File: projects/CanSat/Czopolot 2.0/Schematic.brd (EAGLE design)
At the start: 50.5 x 30.5 mm, 98 parts

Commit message: Microcontroller and sensors done...
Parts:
- removed C40, C41: 100n, Unified:C0603
- removed C43, C44: 10u, Unified:C0603
- removed MOTL, MOTR: MOTOR, Unified:2X_JST
- removed R1, R13: 4.7k, Unified:R0603
- removed R12, R14, R3: 100k, Unified:R0603
- removed R40, R41, R7, R70, R71, R72, R8, R9: 10k, Unified:R0603
- removed R5: 560R, Unified:R0603
- removed RN1: 560R, SobieskiSat2:0603-ARC
- added BTN_USR1: PUSH-SWITCH, SobieskiSat2:SWITCH_SMD
- added U$12: TC78H653FTG, SobieskiSat2:QFN50P300X300X90-17T170N
- added U$13: MOTORJST_SMD, Unified:2X_JSTSMD_F
- added U$16, U$26: RESISTORARRAY, SobieskiSat2:0603-ARC
- added U$17, U$18: CONNECTOR_F_X2_JST_SMD, Unified:2X_JSTSMD_F
- added U$19, U$20, U$24, U$25: CONNECTOR_F_X3_JST_SMD, Unified:3X_JSTSMD_F
- added X1: FH12-24S-0.5SH, con-hirose:FH12-24S-0.5SH
- BAT_PACK: device SobieskiSat2:BAT_THT -> SobieskiSat2:2X_JSTSMD_F
- BTN_DFU: value PUSH-SWITCHDIP -> SLIDE-SWITCH; device SobieskiSat2:2X_JST -> SobieskiSat2:SLIDE-SWITCH
- U$14: value DRV8838 -> MOTORJST_SMD; device SobieskiSat2:SON50P200X200X80-9T90X160N -> Unified:2X_JSTSMD_F
- U$15: value DRV8838 -> RESISTORARRAY; device SobieskiSat2:SON50P200X200X80-9T90X160N -> SobieskiSat2:0603-ARC
- U$4: value SLIDE-SWITCH -> RESISTORARRAY; device SobieskiSat2:SLIDE-SWITCH -> SobieskiSat2:0603-ARC
- U$7: value USB-C -> USB2.0; device SobieskiSat2:USB-C -> SobieskiSat2:USB-C(2)
- moved U$23 35.9 mm to (67.8, 25.8)
- moved LM3940IMP 35.6 mm to (46.0, 18.8), flipped to the bottom, turned to 90 degrees
- moved U$14 34.6 mm to (35.8, 3.50), flipped to the bottom, turned to 180 degrees
- moved BAT_PACK 34.3 mm to (58.5, 3.75)
- moved U$22 33.9 mm to (67.8, 21.4)
- moved LEDA 33.6 mm to (4.75, 28.8), turned to 0 degrees
- moved C31 33.4 mm to (43.5, 13.2)
- moved C30 32.2 mm to (51.2, 17.2), turned to 90 degrees
- moved LEDB 31.9 mm to (6.75, 28.8), turned to 0 degrees
- moved C2 31.6 mm to (49.0, 13.2), flipped to the bottom, turned to 0 degrees
- moved C10 30.8 mm to (50.0, 14.5), turned to 0 degrees
- moved CBK 30.6 mm to (2.00, 25.5), flipped to the top, turned to 90 degrees
- moved LEDC 30.3 mm to (8.75, 28.8), turned to 0 degrees
- moved C23 30.2 mm to (46.0, 10.5)
- moved C21 29.6 mm to (54.8, 20.0)
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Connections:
- removed net EN_L: U$1.15, U$14.5
- removed net EN_R: U$1.17, U$15.5
- removed net GPIO_S1: U$1.26, U$11.6
- removed net GPIO_S2: U$1.27, U$11.10
- removed net N$23: C70.2, U$9.10
- removed net N$31: R40.1, U$14.7
- removed net N$34: MOTR.P$2, U$15.2
- removed net N$36: MOTR.P$1, U$15.3
- removed net N$40: R41.1, U$15.7
- removed net PH_L: U$1.14, U$14.6
- removed net PH_R: U$1.16, U$15.6
- new net EN_1: U$1.33
- new net EN_2: U$1.34
- new net EN_3: U$1.35
- new net EN_4: U$1.36
- new net MPU_REG: C70.2, U$9.10, U$9.14
- new net N$25: R0.1
- new net N$7: BTN_USR.P$1, BTN_USR.P$4, U$16.4
- new net PWM_1: U$1.27
- new net PWM_2: U$1.26
- new net PWM_3: U$1.37
- new net PWM_4: U$1.38
- net 43_D0: now also U$1.24; no longer U$1.25
- net 43_D1: now also U$1.25; no longer U$1.24
- net 43_MOSI: now also U$26.8; no longer R3.2
- net 43_NSS: now also U$1.2; no longer U$1.61
- net 43_RST: now also U$1.50; no longer R2.2, U$1.28
- net BAT: now also BAT_PACK.+; no longer BAT_PACK.P$2, C40.2, C43.2, U$14.1, U$15.1
- net BMP_SDI: now also U$26.7; no longer R9.1
- net BMP_SDO: now also U$26.6; no longer R8.2
- net DFU: now also U$16.7; no longer BTN_DFU.P$2, R12.1
- net GND: now also BAT_PACK.-, U$7.A1, U$7.A12, U$7.B1, U$7.B12, U$7.MID@1, U$7.MID@2, U$9.5; no longer BAT_PACK.P$1, BTN_USR.P$1, BTN_USR.P$4, C40.1, C41.1, C43.1, C44.1, R0.1, R12.2, R8.1, U$14.4, U$14.9, U$15.4, U$15.9, U$7.A$1, U$7.A$12, U$7.B$1, U$7.B$12, U$7.N$1, U$7.N$2, U$7.N$3, U$7.N$4, U$7.N$5, U$7.N$6
- net GPIO_RX: no longer U$1.38
- net GPIO_TX: no longer U$1.37
- net IMU_INT: no longer U$1.62
- net MPU_AD0: now also U$15.8, U$9.15; no longer R72.1
- net MPU_NCS: now also U$15.7; no longer R7.1
- net N$1: now also U$4.1; no longer RN1.7
- net N$10: no longer RN1.1
- net N$15: now also U$1.8, U$4.5; no longer R5.2, U$1.36
- net N$16: now also BTN_USR1.P$1, BTN_USR1.P$4, U$16.6; no longer BTN_USR.P$2, BTN_USR.P$3, R1.1
- net N$19: now also U$1.11, U$4.8; no longer RN1.4, U$1.35
- net N$2: now also U$4.2; no longer RN1.6
- net N$20: now also U$1.10, U$4.7; no longer RN1.3, U$1.34
- net N$26: now also U$1.9, U$4.6; no longer MOTL.P$1, U$14.3
- net N$28: now also BTN_USR1.P$2, BTN_USR1.P$3, U$1.61; no longer RN1.2, U$1.33
- net N$3: no longer RN1.8
- net N$37: now also U$4.3; no longer RN1.5
- net N$38: now also U$4.4; no longer R5.1
- net N$4: now also R2.2, U$1.28; no longer R1.2, U$1.50
- net N$5: now also BTN_USR.P$2, BTN_USR.P$3, U$1.62; no longer MOTL.P$2, U$14.2
- net NRST: now also U$26.5; no longer R13.1
- net SCL: now also U$15.6, U$9.3; no longer R71.1
- net SDA: now also U$15.5, U$9.2; no longer R70.1
- net SD_D3: now also U$16.8; no longer R14.2
- net USB_D+: now also U$7.A6, U$7.B6; no longer U$7.A$6, U$7.B$6
- net USB_D-: now also U$7.A7, U$7.B7; no longer U$7.A$7, U$7.B$7
- net USB_VBUS: now also U$7.A4, U$7.A9, U$7.B4, U$7.B9; no longer U$7.A$4, U$7.A$9, U$7.B$4, U$7.B$9
- net VCC: now also U$15.1, U$15.2, U$15.3, U$15.4, U$16.1, U$16.2, U$16.3, U$16.5, U$26.1, U$26.2, U$26.3, U$26.4; no longer BTN_DFU.P$1, C41.2, C44.2, LEDP.A, R13.2, R14.1, R3.1, R40.2, R41.2, R7.2, R70.2, R71.2, R72.2, R9.2, U$14.8, U$15.8
- net VSYS: now also LEDP.A
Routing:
- net GND: track 163.3 -> 23.3 mm, vias 0 -> 3
- net VCC: track 124.7 -> 59.8 mm, vias 6 -> 1
- net BAT: track 58.7 -> 0.00 mm
- net GPIO_SCL: track 30.8 -> 0.00 mm, vias 1 -> 0
- net USB_D+: track 35.8 -> 6.59 mm, vias 3 -> 0
- net USB_D-: track 33.3 -> 6.53 mm, vias 2 -> 0
- net GPIO_S2: track 26.5 -> 0.00 mm, vias 1 -> 0
- net GPIO_RX: track 26.3 -> 0.00 mm, vias 1 -> 0
- net GPIO_S1: track 25.5 -> 0.00 mm, vias 1 -> 0
- net GPIO_TX: track 25.5 -> 0.00 mm, vias 1 -> 0
- net GPIO_SDA: track 23.4 -> 0.00 mm, vias 1 -> 0
- net GPIO_MOSI: track 23.1 -> 0.00 mm, vias 1 -> 0
- net VSYS: track 22.7 -> 0.00 mm
- net GPIO_MISO: track 22.5 -> 0.00 mm, vias 1 -> 0
- net GPIO_SCK: track 21.8 -> 0.00 mm, vias 1 -> 0
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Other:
- board size 50.5 x 30.5 mm -> 53 x 31.8 mm
- board text removed: "X"
- board text removed: "Y"
- board text removed: "Z"

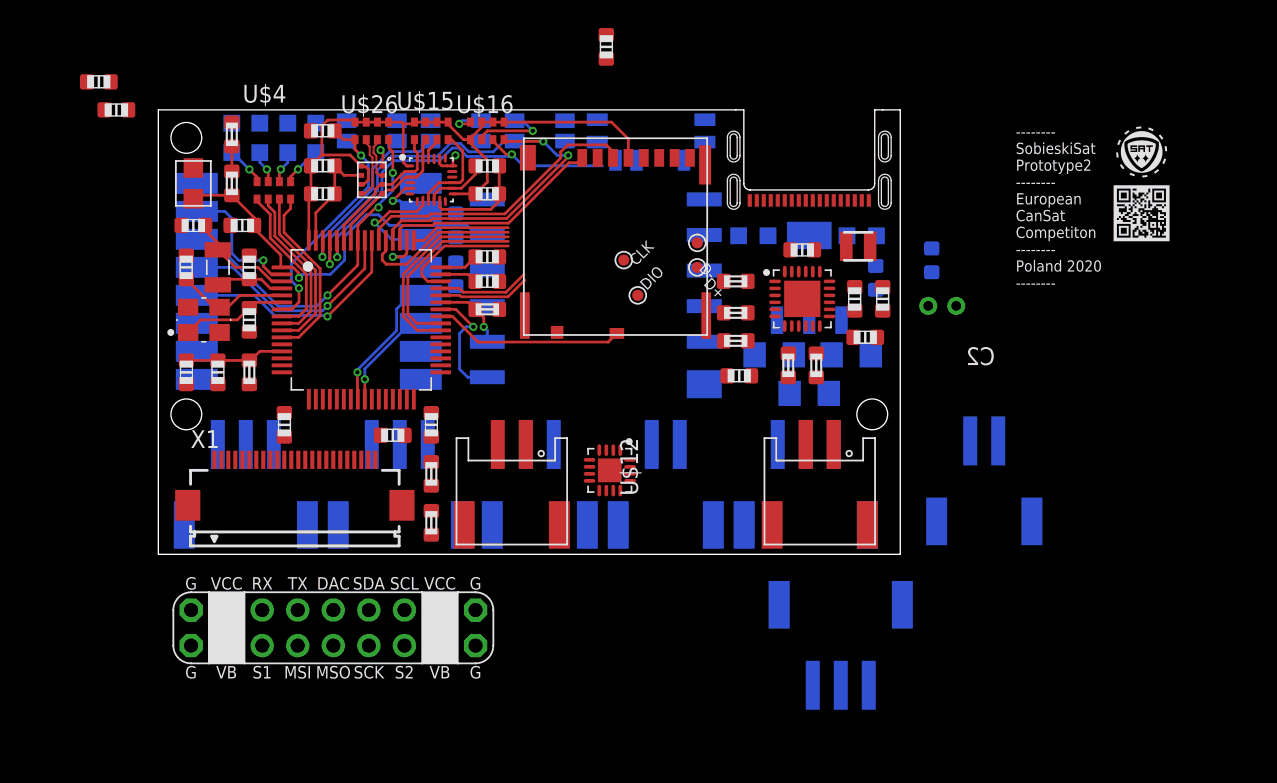
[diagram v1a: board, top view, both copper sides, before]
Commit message: Dual motor connectors added
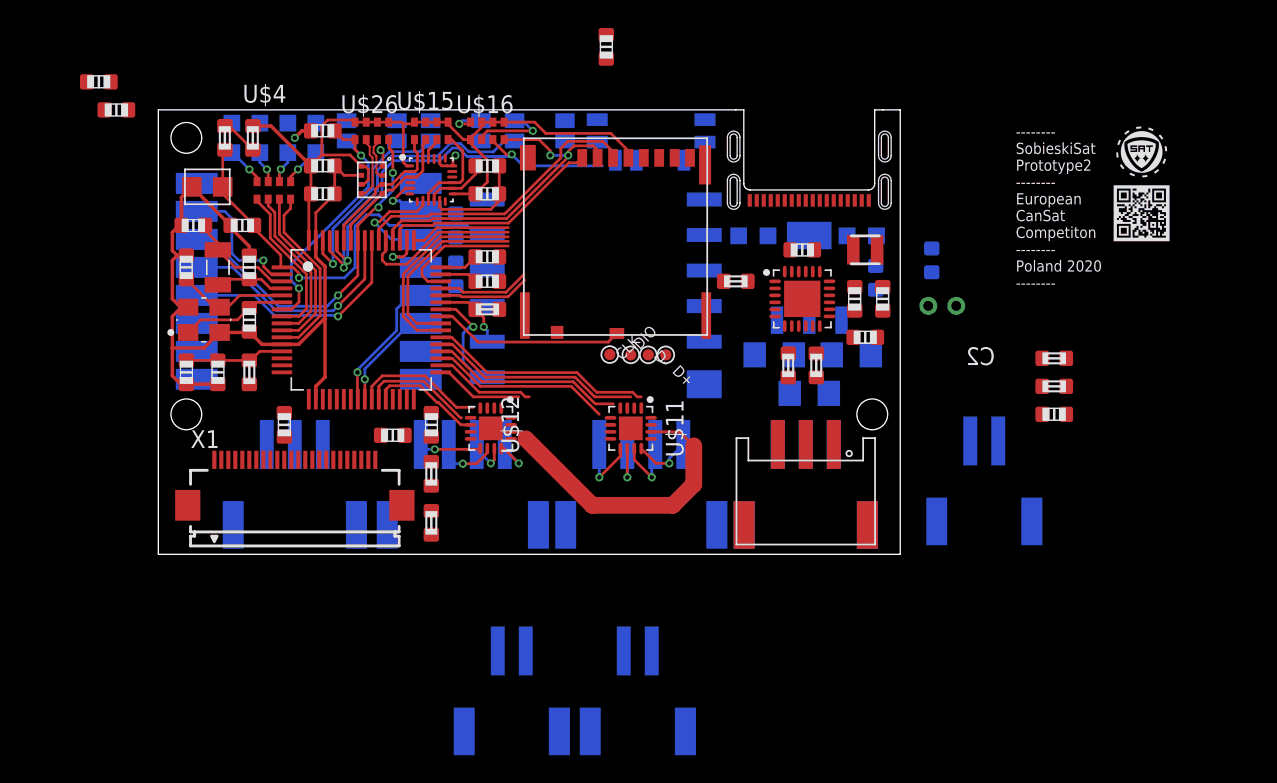
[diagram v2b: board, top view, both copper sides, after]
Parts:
- removed U$25: CONNECTOR_F_X3_JST_SMD, Unified:3X_JSTSMD_F
- U$11: value GPIO_PADS2 -> TC78H653FTG; device SobieskiSat2:GPIO_PADS2 -> SobieskiSat2:QFN50P300X300X90-17T170N
- U$17, U$18: value CONNECTOR_F_X2_JST_SMD -> CONNECTOR_F_X4_JST_SMD; device Unified:2X_JSTSMD_F -> Unified:4X_JSTSMD_F
- moved U$19 40.0 mm to (45.8, 3.50), flipped to the top
- moved U$11 25.6 mm to (33.2, 8.00), turned to 270 degrees
- moved U$17 25.5 mm to (21.2, 3.50), flipped to the bottom
- moved R22 23.0 mm to (63.5, 13.0)
- moved R23 23.0 mm to (63.5, 11.0)
- moved C20 22.7 mm to (63.5, 9.00)
- moved U$13 14.9 mm to (24.8, -11.2)
- moved U$14 14.9 mm to (33.8, -11.2)
- moved U$18 9.25 mm to (34.0, 3.50), flipped to the bottom
- moved U$12 9.01 mm to (23.2, 8.00)
- moved D- 8.73 mm to (34.5, 13.2)
- moved U$20 7.50 mm to (9.25, 3.50)
- moved CLK 6.82 mm to (31.8, 13.3)
- moved D+ 6.64 mm to (35.8, 13.2)
- moved DIO 4.28 mm to (33.2, 13.2)
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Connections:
- net EN_3 renamed P_EN_3
- net EN_4 renamed P_EN_4
- removed net GPIO_RX: U$11.1
- removed net GPIO_TX: U$11.2
- new net MOT_STBY: R2.2, U$1.28, U$11.6, U$12.6
- new net N$23: U$11.10, U$18.P$2
- new net N$29: U$11.11, U$18.P$3
- new net N$30: U$11.12, U$18.P$4
- new net N$31: U$12.9, U$17.P$1
- new net N$33: U$12.10, U$17.P$2
- new net N$34: U$12.11, U$17.P$3
- new net N$35: U$12.12, U$17.P$4
- net BAT: now also U$11.14, U$12.14; no longer U$11.VBAT$1, U$11.VBAT$2
- net GND: now also U$11.13, U$11.17, U$11.8, U$12.13, U$12.17, U$12.8; no longer U$11.GND, U$11.GND$1, U$11.GND$2, U$11.GND$3
- net GPIO_DAC: no longer U$11.3
- net GPIO_MISO: no longer U$11.8
- net GPIO_MOSI: no longer U$11.7
- net GPIO_SCK: no longer U$11.9
- net GPIO_SCL: no longer U$11.5
- net GPIO_SDA: no longer U$11.4
- net N$4: now also U$11.9, U$18.P$1; no longer R2.2, U$1.28
- net VCC: no longer U$11.VCC$1, U$11.VCC$2
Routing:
- net GND: track 23.3 -> 75.8 mm, vias 3 -> 4
- net BAT: track 0.00 -> 22.1 mm
- net PWM_4: track 0.00 -> 16.1 mm
- net PWM_3: track 0.00 -> 15.1 mm
- net P_EN_4: track 0.00 -> 13.9 mm
- net P_EN_3: track 0.00 -> 13.0 mm
- net PWM_2: track 0.00 -> 9.41 mm
- net PWM_1: track 0.00 -> 8.07 mm
- net MOT_STBY: track 0.00 -> 8.02 mm
- net EN_2: track 0.00 -> 7.26 mm
- net EN_1: track 0.00 -> 6.30 mm
- net N$4: track 0.00 -> 5.03 mm, vias 0 -> 1
- net N$29: track 0.00 -> 5.03 mm, vias 0 -> 1
- net VCC: track 59.8 -> 64.6 mm
- net N$33: track 0.00 -> 4.75 mm, vias 0 -> 1
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
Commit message: V2 work...
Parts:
- removed THR: NTC, SobieskiSat2:NTC
- added C17, C18: 100n, Unified:C0603
- added GND, VCC: PADTEST, Unified:TESTPAD
- added R1, R5: 10k, Unified:R0603
- added R3, R7: 10k, SobieskiSat2:DR0603
- added R8: 1k, Unified:R0603
- added U$25: GPIO_PADS, SobieskiSat2:GPIO_PADS
- moved C20 20.7 mm to (44.5, 17.2), turned to 90 degrees
- moved DIO 19.5 mm to (40.2, 31.5)
- moved CLK 18.8 mm to (35.2, 31.8)
- moved R22 17.8 mm to (46.2, 17.2), turned to 90 degrees
- moved R23 17.2 mm to (46.5, 13.8), turned to 90 degrees
- moved BAT_PACK 14.8 mm to (73.2, 3.75)
- moved D+ 12.9 mm to (41.0, 25.0)
- moved R2 11.7 mm to (27.5, 9.25), turned to 180 degrees
- moved D- 10.7 mm to (24.5, 17.0)
- moved R4 9.55 mm to (12.2, 11.5), flipped to the bottom, turned to 0 degrees
- moved R20 7.00 mm to (46.5, 22.5), turned to 270 degrees
- moved C21 5.86 mm to (50.2, 23.8), turned to 0 degrees
- moved U$13 4.96 mm to (21.0, -8.00)
- moved C22 4.70 mm to (49.8, 22.8)
- moved L2 4.70 mm to (54.2, 22.8)
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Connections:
- removed net GPS_RST: U$3.10
- removed net N$22: R22.1, R23.2, R24.1, THR.P$1
- removed net N$25: R0.1
- new net N$36: R1.2, U$12.16
- new net N$39: R3.1, U$12.15
- new net N$40: R5.2, U$11.16
- new net N$42: R7.1, U$11.15
- new net NTC: R22.1, R23.2, R24.1, U$24.P$3
- new net UART2_RX: U$1.17, X1.6
- new net UART2_TX: U$1.16, X1.5
- new net UART4_RX: U$1.15, X1.4
- new net UART4_TX: U$1.14, X1.3
- net BAT: now also C17.1, C18.1, U$19.P$2, U$20.P$2, U$24.P$2, X1.21, X1.22
- net DFU: now also U$3.10
- net EN_1: now also U$12.5, X1.13
- net EN_2: now also U$12.1, X1.14
- net GND: now also C17.2, C18.2, GND.PAD, R0.1, R3.3, R7.3, U$19.P$1, U$20.P$1, U$24.P$1, X1.1, X1.17, X1.23, X1.7; no longer THR.P$2
- net GPIO_DAC: now also X1.9
- net GPIO_MISO: now also X1.11
- net GPIO_MOSI: now also X1.12
- net GPIO_SCK: now also X1.10
- net GPIO_SCL: now also X1.20
- net GPIO_SDA: now also X1.19
- net N$10: now also R8.1
- net N$3: now also R8.2
- net PWM_1: now also U$12.2, X1.16
- net PWM_2: now also U$12.4, X1.15
- net PWM_3: now also U$11.2
- net PWM_4: now also U$11.4
- net P_EN_3: now also U$11.5
- net P_EN_4: now also U$11.1
- net VCC: now also R1.1, R3.2, R5.1, R7.2, VCC.PAD, X1.18, X1.2, X1.24, X1.8
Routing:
- net GND: track 75.8 -> 136.0 mm, vias 4 -> 5
- net BAT: track 22.1 -> 79.9 mm, vias 0 -> 3
- net VCC: track 64.6 -> 118.3 mm, vias 1 -> 3
- net USB_D+: track 6.59 -> 47.6 mm, vias 0 -> 3
- net USB_D-: track 6.53 -> 46.9 mm, vias 0 -> 3
- net SWDIO: track 8.85 -> 31.1 mm
- net USB_VBUS: track 0.00 -> 21.2 mm
- net VSYS: track 0.00 -> 17.2 mm, vias 0 -> 2
- net SD_D1: track 13.5 -> 28.9 mm
- net DFU: track 28.1 -> 43.4 mm
- net SWCLK: track 7.13 -> 21.7 mm
- net MOT_STBY: track 8.02 -> 22.5 mm, vias 0 -> 2
- net SD_D0: track 14.7 -> 28.8 mm
- net NTC: track 0.00 -> 13.1 mm, vias 0 -> 1
- net SD_CLK: track 11.6 -> 24.5 mm
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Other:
- board size 53 x 31.8 mm -> 57 x 32.8 mm

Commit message: V2 almost done
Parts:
- removed BAT_PACK: (no value), SobieskiSat2:2X_JSTSMD_F
- removed CLK, D+, D-, DIO, GND, VCC: PADTEST, Unified:TESTPAD
- removed U$18: CONNECTOR_F_X4_JST_SMD, Unified:4X_JSTSMD_F
- removed U$24: CONNECTOR_F_X3_JST_SMD, Unified:3X_JSTSMD_F
- added C19, C25: 10u, Unified:C1206
- added C26, C27: 50p, Unified:C0603
- added C28: (no value), rcl:153CLV-0405
- added R10, R9: 0R, Unified:R0603
- C2, C23: device Unified:C1206 -> Unified:C0603
- U$13: value MOTORJST_SMD -> MOTOR_DUO; device Unified:2X_JSTSMD_F -> SobieskiSat2:4(2)X_JSTSMD_F
- U$14: value MOTORJST_SMD -> BAT_JST_4(3); device Unified:2X_JSTSMD_F -> SobieskiSat2:4(3)X_JSTSMD_F
- U$17: value CONNECTOR_F_X4_JST_SMD -> MOTOR_DUO; device Unified:4X_JSTSMD_F -> SobieskiSat2:4(2)X_JSTSMD_F
- U$25: value GPIO_PADS -> GPIO_DEBUG; device SobieskiSat2:GPIO_PADS -> SobieskiSat2:GPIO_DEBUG
- X1: device con-hirose:FH12-24S-0.5SH -> SobieskiSat2:FH12-24S-0.5SH
- moved U$14 20.6 mm to (50.2, 4.50)
- moved U$13 18.8 mm to (35.0, 4.50)
- moved C80 13.9 mm to (9.00, 30.5), turned to 90 degrees
- moved C16 9.75 mm to (40.5, 30.8), turned to 270 degrees
- moved R30 9.74 mm to (46.5, 23.8), turned to 180 degrees
- moved R8 9.50 mm to (54.0, 23.8), turned to 180 degrees
- moved LEDCH 9.17 mm to (55.2, 20.8), turned to 0 degrees
- moved LEDP 9.17 mm to (45.2, 20.8), turned to 0 degrees
- moved C2 7.04 mm to (59.5, 16.8), turned to 270 degrees
- moved C10 6.50 mm to (60.2, 12.2)
- moved R4 5.77 mm to (14.0, 6.00), turned to 270 degrees
- moved C23 5.62 mm to (55.0, 14.0), flipped to the top, turned to 270 degrees
- moved C20 5.34 mm to (45.5, 22.5), turned to 270 degrees
- moved R20 4.12 mm to (45.5, 18.5)
- moved R22 3.34 mm to (45.5, 14.0)
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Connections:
- new net BAT_BQ: C23.1, R9.2, U$10.11, U$10.12
- new net GPS_RST: R10.2, U$3.10
- new net N$25: BTN_DFU.P$1, R10.1
- net BAT: now also C19.1, C25.1, C26.1, C27.1, R1.1, R3.2, R5.1, R7.2, R9.1, U$14.BAT; no longer BAT_PACK.+, C23.1, U$10.11, U$10.12, U$24.P$2, X1.21, X1.22
- net DFU: now also BTN_DFU.P$3, X1.14; no longer U$3.10
- net EN_1: now also X1.15; no longer X1.13
- net EN_2: now also X1.16; no longer X1.14
- net GND: now also BTN_DFU.P$2, C19.2, C25.2, C26.2, C27.2, U$13.S$1, U$13.S$2, U$13.S$3, U$13.S$4, U$14.GND, U$14.S$1, U$14.S$2, U$14.S$3, U$17.S$1, U$17.S$2, U$17.S$3, U$17.S$4, U$19.S$1, U$19.S$2, U$20.S$1, U$20.S$2, U$25.P$1, U$25.P$9, X1.S$1, X1.S$2; no longer BAT_PACK.-, GND.PAD, U$24.P$1
- net GPIO_SCL: now also X1.22; no longer X1.20
- net GPIO_SDA: now also X1.21; no longer X1.19
- net N$23: now also U$13.P$2; no longer U$18.P$2
- net N$29: now also U$13.P$3; no longer U$18.P$3
- net N$30: now also U$13.P$4; no longer U$18.P$4
- net N$4: now also U$13.P$1; no longer U$18.P$1
- net NRST: now also X1.13
- net NTC: now also U$14.NTC; no longer U$24.P$3
- net PWM_1: now also X1.20; no longer X1.16
- net PWM_2: now also X1.19; no longer X1.15
- net PWM_3: now also U$25.P$7
- net PWM_4: now also U$11.1, U$25.P$8; no longer U$11.4
- net P_EN_4: now also U$11.4; no longer U$11.1
- net SWCLK: now also U$25.P$3; no longer CLK.PAD
- net SWDIO: now also U$25.P$2; no longer DIO.PAD
- net UART2_RX: now also U$20.P$3
- net UART2_TX: now also U$19.P$3
- net USB_D+: now also U$25.P$4; no longer D+.PAD
- net USB_D-: now also U$25.P$5; no longer D-.PAD
- net VCC: now also LEDP.A, U$25.P$6; no longer LEDCH.A, R1.1, R3.2, R5.1, R7.2, VCC.PAD
- net VSYS: now also LEDCH.A, U$14.AUX; no longer LEDP.A
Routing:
- net VCC: track 118.3 -> 182.7 mm, vias 3 -> 6
- net UART2_TX: track 8.17 -> 62.1 mm, vias 0 -> 2
- net GND: track 136.0 -> 105.5 mm, vias 5 -> 19
- net BAT: track 79.9 -> 105.8 mm, vias 3 -> 7
- net NRST: track 18.7 -> 41.2 mm, vias 2 -> 5
- net MOT_STBY: track 22.5 -> 35.2 mm
- net PWM_3: track 17.3 -> 29.8 mm, vias 0 -> 2
- net GPS_RST: track 0.00 -> 12.3 mm
- net PWM_4: track 22.7 -> 30.8 mm, vias 2 -> 0
- net SWCLK: track 21.7 -> 29.1 mm, vias 0 -> 2
- net N$10: track 3.71 -> 11.0 mm
- net N$29: track 2.17 -> 8.89 mm, vias 1 -> 2
- net USB_VBUS: track 21.2 -> 14.7 mm
- net N$21: track 8.84 -> 2.64 mm, vias 1 -> 0
- net N$30: track 1.36 -> 7.55 mm, vias 1 -> 2
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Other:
- board text removed: "A"
- board text removed: "B"
- board text removed: "C"
- board text removed: "CH"
- board text removed: "D"
- board text removed: "DFU"
- board text removed: "PWR"
- board text removed: "USR"

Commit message: GND yet to fix
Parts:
- moved C81 68.8 mm to (64.0, 17.0), turned to 270 degrees
- moved C16 9.30 mm to (31.2, 30.9), turned to 90 degrees
- moved C10 7.46 mm to (66.0, 17.0), turned to 270 degrees
- moved C2 2.51 mm to (62.0, 17.0), flipped to the top
- moved BTN_DFU 1.75 mm to (35.8, 31.0)
- moved R10 1.50 mm to (40.2, 30.8)
- moved C25 0.75 mm to (41.5, 4.75), turned to 180 degrees
- moved C18 0.50 mm to (41.5, 8.00)
- moved C26 0.50 mm to (39.5, 8.00)
- moved L2 0.35 mm to (54.5, 22.5)
- moved R1 0.25 mm to (28.5, 10.8)
- moved R3 0.25 mm to (28.5, 13.0)
- moved R5 0.25 mm to (39.0, 10.8)
- moved R7 0.25 mm to (38.2, 13.0)
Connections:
- net BAT: now also C28.+, U$19.S$1, U$19.S$2
- net GND: now also C28.-; no longer U$19.S$1, U$19.S$2
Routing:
- net BAT: track 105.8 -> 157.2 mm
- net VCC: track 182.7 -> 204.3 mm, vias 6 -> 12
- net VSYS: track 21.0 -> 33.5 mm
- net BAT_BQ: track 4.69 -> 17.0 mm
- net UART2_TX: track 62.1 -> 71.2 mm
- net N$21: track 2.64 -> 9.75 mm
- net N$29: track 8.89 -> 15.2 mm
- net N$23: track 8.29 -> 14.2 mm
- net N$34: track 8.29 -> 13.8 mm
- net N$33: track 8.49 -> 13.7 mm
- net USB_VBUS: track 14.7 -> 19.8 mm
- net N$30: track 7.55 -> 11.8 mm
- net N$35: track 7.55 -> 11.5 mm
- net N$31: track 7.56 -> 10.5 mm
- net N$4: track 7.55 -> 10.5 mm
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- added copper zone on layer 1, net GND
- added copper zone on layer 16, net GND

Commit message: Extension board
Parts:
- added U$18: LOGOSQSM, SobieskiSat2:LOGOSQSM
- moved U$22 37.8 mm to (30.8, 19.0), flipped to the bottom
- moved U$23 37.8 mm to (30.8, 23.4), flipped to the bottom
- moved U$25 2.50 mm to (42.8, 24.8)
- moved R9 1.27 mm to (54.2, 14.2), turned to 180 degrees
- moved U$20 0.75 mm to (7.75, 4.50)
- moved R4 0.45 mm to (14.4, 6.25)
- moved C28 0.25 mm to (50.2, 12.8)
- moved C8 0.25 mm to (17.2, 9.50)
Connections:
- net GND: now also U$7.S$1, U$7.S$2, U$7.S$3, U$7.S$4, U$7.S$5, U$7.S$6, U$7.S$7, U$7.S$8, X1.18, X1.24; no longer U$25.P$9, X1.17, X1.23
- net PWM_3: no longer U$25.P$7
- net PWM_4: no longer U$25.P$8
- net VCC: now also X1.17, X1.23; no longer X1.18, X1.24
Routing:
- net PWM_4: track 30.8 -> 20.6 mm
- net PWM_3: track 29.7 -> 19.9 mm, vias 2 -> 0
- net VCC: track 204.3 -> 209.5 mm
- net GND: track 105.4 -> 110.3 mm, vias 65 -> 66
- net BAT: track 157.2 -> 155.0 mm
- net SWDIO: track 29.3 -> 30.4 mm
- net VSYS: track 33.5 -> 34.6 mm
- net GPIO_SCL: track 8.66 -> 9.67 mm
- net BAT_BQ: track 17.0 -> 16.5 mm
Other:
- outline, holes or cut-outs redrawn
- board text added: "-------- SobieskiSat Prototype3 -------- European CanSat Competiton -------- Poland 2020 --------"
- board text added: "European CanSat Competiton"
- board text added: "L=4, H=2 channels"
- board text added: "OPPO FLEX!"
- board text added: "SobieskiSat Prototype3"
- board text removed: "-------- SobieskiSat Prototype2 -------- European CanSat Competiton -------- Poland 2020 --------"
